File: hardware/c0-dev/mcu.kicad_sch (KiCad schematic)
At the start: 43 parts, among them J15 TAG_CONNECT, J17 PinHeader_2.54mm, U7 TCA9555PWR, U8 W25Q128JVP, U9 RP2350A, Y1 ABM8-272-T3 (12Mhz)

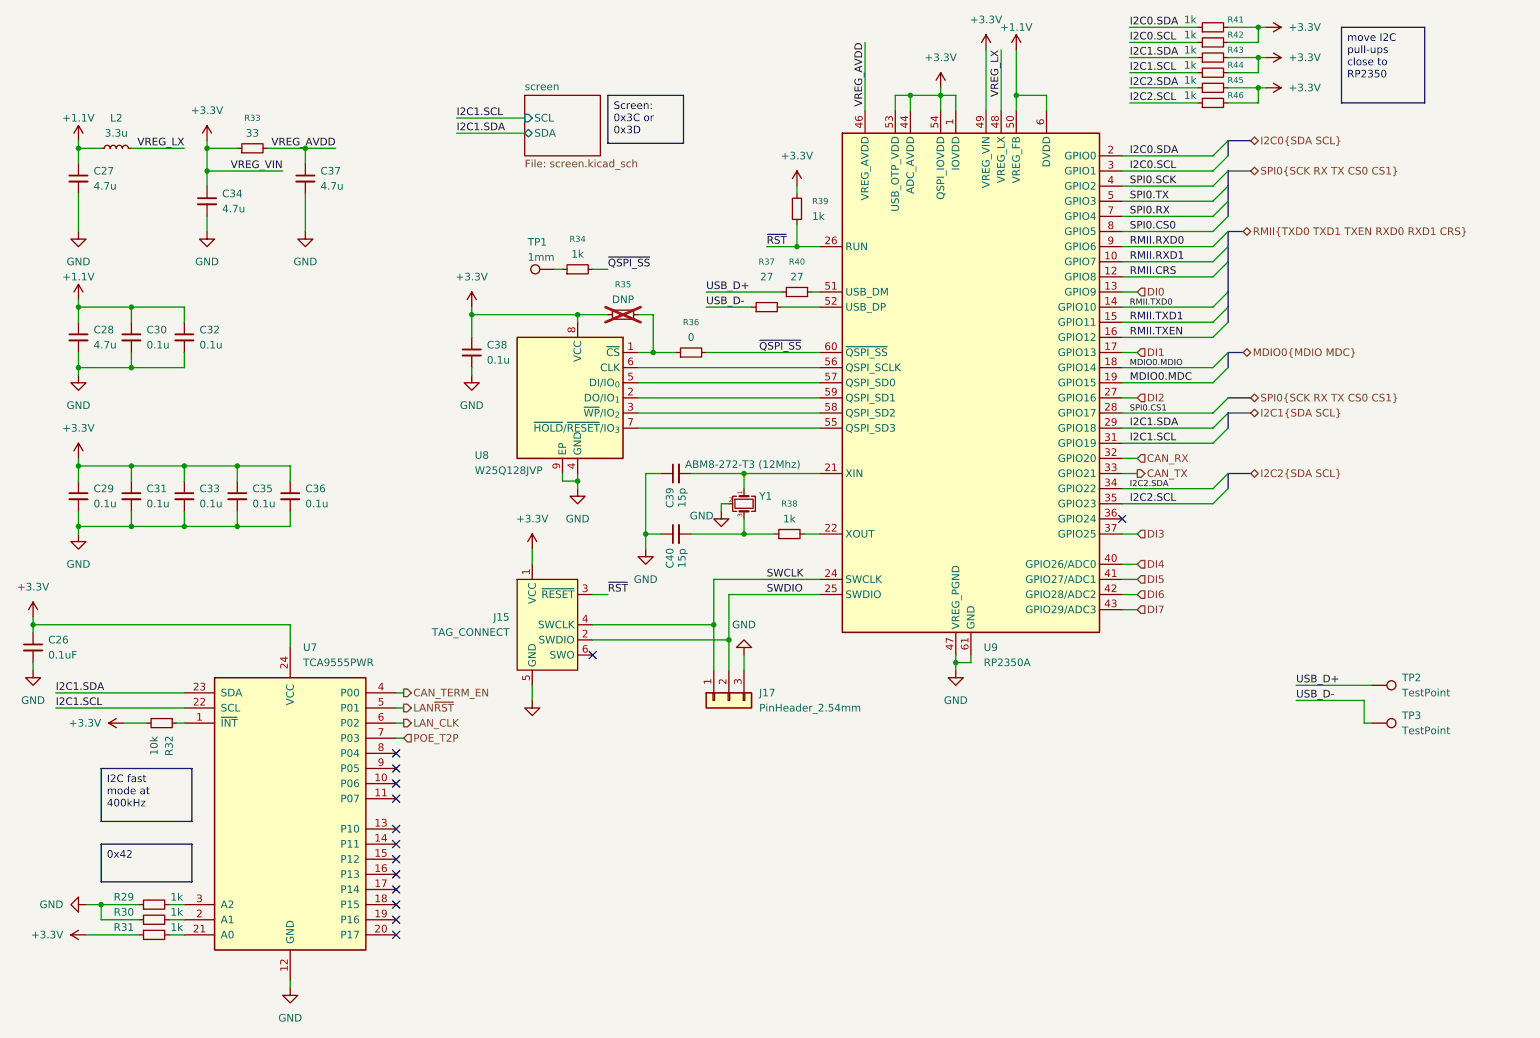
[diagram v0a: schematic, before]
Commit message: added watchdog
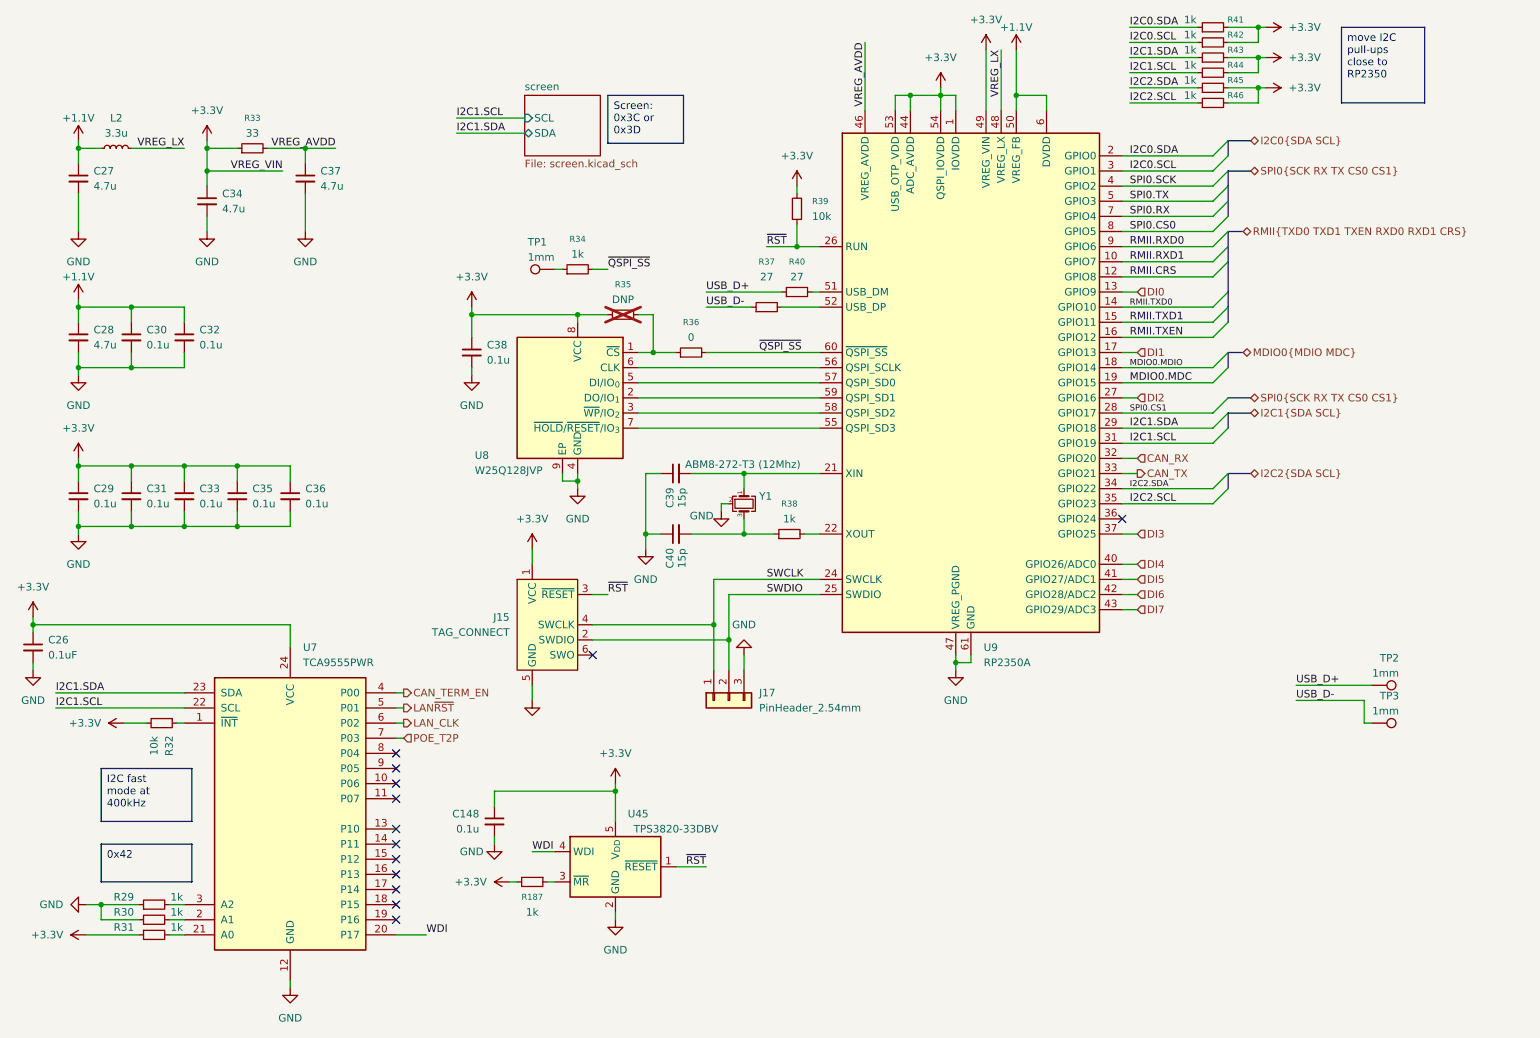
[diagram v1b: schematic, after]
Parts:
- added C148: 0.1u, Capacitor_SMD:C_0402_1005Metric, symbol Device:C_Small
- added R187: 1k, Resistor_SMD:R_0402_1005Metric, symbol Device:R_Small
- added U45: TPS3820-33DBV, Package_TO_SOT_SMD:SOT-23-5, symbol Power_Supervisor:TPS3823-xxDBV
- R39: value 1k -> 10k
- TP2, TP3: value TestPoint -> 1mm; footprint TestPoint:TestPoint_Pad_D2.0mm -> TestPoint:TestPoint_Pad_D1.0mm
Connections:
- net +3.3V: now also C148.1, R187.2, U45.5 (V_{DD})
- net GND: now also C148.2, U45.2 (GND)
- net ~{RST}: now also U45.1 (~{RESET})
- net WDI: now reaches U7.20 (P17)
- net WDI: now also U45.4 (WDI)
- new net: R187.1, U45.3 (~{MR})
- no-connect marks 14 -> 13

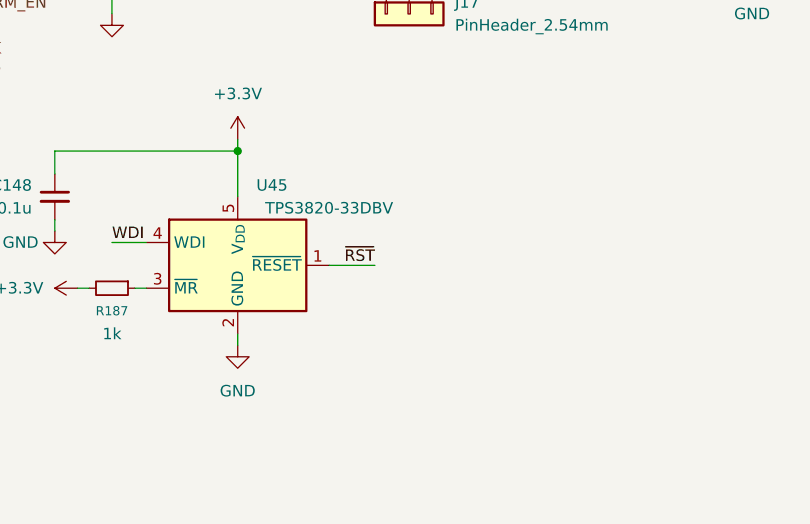
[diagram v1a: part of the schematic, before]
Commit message: added watchdog output disable
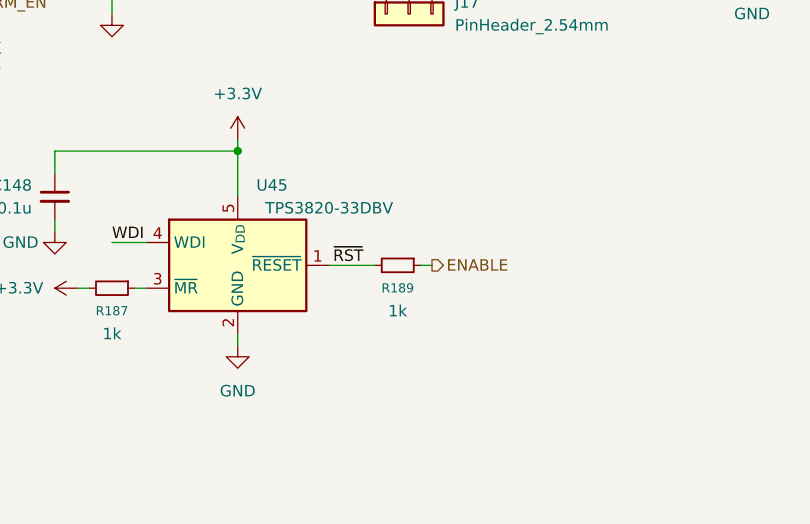
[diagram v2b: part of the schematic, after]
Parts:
- added R189: 1k, Resistor_SMD:R_0402_1005Metric, symbol Device:R_Small
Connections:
- net ~{RST}: now also R189.2
- new net ENABLE: R189.1
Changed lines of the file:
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@@
 	(wire
 		(pts
+			(xy 153.67 163.83) (xy 154.94 163.83)
+		)
+		(stroke
+			(width 0)
+			(type default)
+		)
+	)
+	(wire
+		(pts
 			(xy 219.71 22.86) (xy 231.14 22.86)
 		)
@@
 		)
 	)
+	(label "~{RST}"
+		(at 147.32 163.83 180)
+		(effects
+			(font
+				(size 1.27 1.27)
+			)
+			(justify right bottom)
+		)
+	)
 	(label "I2C1.SCL"
 		(at 219.71 30.48 0)
@@
 		)
 	)
-	(label "~{RST}"
-		(at 148.59 163.83 180)
-		(effects
-			(font
-				(size 1.27 1.27)
-			)
-			(justify right bottom)
-		)
-	)
 	(hierarchical_label "MDIO0{MDIO MDC}"
 		(shape bidirectional)
@@
 		)
 	)
+	(hierarchical_label "ENABLE"
+		(shape output)
+		(at 154.94 163.83 0)
+		(effects
+			(font
+				(size 1.27 1.27)
+			)
+			(justify left)
+		)
+	)
 	(hierarchical_label "CAN_TERM_EN"
 		(shape output)
@@
 					(unit 1)
 				)
+			)
+		)
+	)
+	(symbol
+		(lib_id "Device:R_Small")
+		(at 151.13 163.83 270)
+		(unit 1)
+		(body_style 1)
+		(exclude_from_sim no)
+		(in_bom yes)
+		(on_board yes)
+		(in_pos_files yes)
+		(dnp no)
+		(property "Reference" "R189"
+			(at 151.13 166.37 90)
+			(show_name no)
+			(do_not_autoplace no)
+			(effects
+				(font
+					(size 1.016 1.016)
+				)
+			)
+		)
+		(property "Value" "1k"
+			(at 151.13 168.91 90)
+			(show_name no)
+			(do_not_autoplace no)
+			(effects
+				(font
+					(size 1.27 1.27)
+				)
+			)
+		)
+		(property "Footprint" "Resistor_SMD:R_0402_1005Metric"
+			(at 151.13 163.83 0)
+			(hide yes)
+			(show_name no)
+			(do_not_autoplace no)
+			(effects
+				(font
+					(size 1.27 1.27)
+				)
+			)
+		)
+		(property "Datasheet" ""
+			(at 151.13 163.83 0)
+			(hide yes)
+			(show_name no)
+			(do_not_autoplace no)
+			(effects
+				(font
+					(size 1.27 1.27)
+				)
+			)
+		)
+		(property "Description" "Resistor, small symbol"
+			(at 151.13 163.83 0)
+			(hide yes)
+			(show_name no)
+			(do_not_autoplace no)
+			(effects
+				(font
+					(size 1.27 1.27)
+				)
+			)
+		)
+		(pin "2"
+		)
+		(pin "1"
+		)
+		(instances
+			(project "c0-dev"
+				(path "/b8347a0e-ad04-4414-969d-3c64a611d74e/b3a362d3-bb15-48bf-a1e5-1773c27a02b7"
+					(reference "R189")
+					(unit 1)
+				)

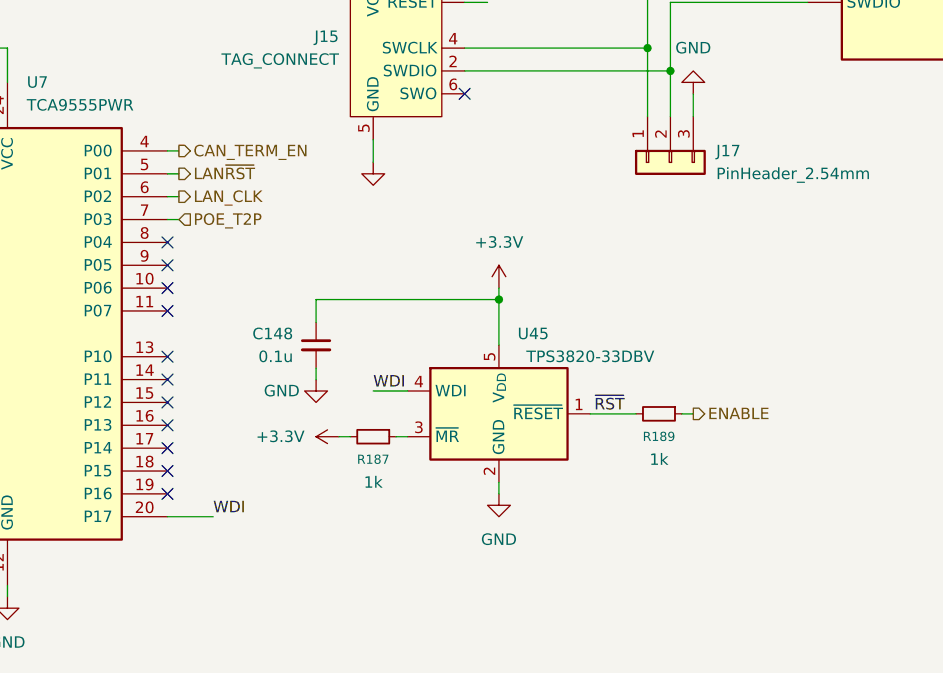
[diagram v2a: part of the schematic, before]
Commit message: added status leds
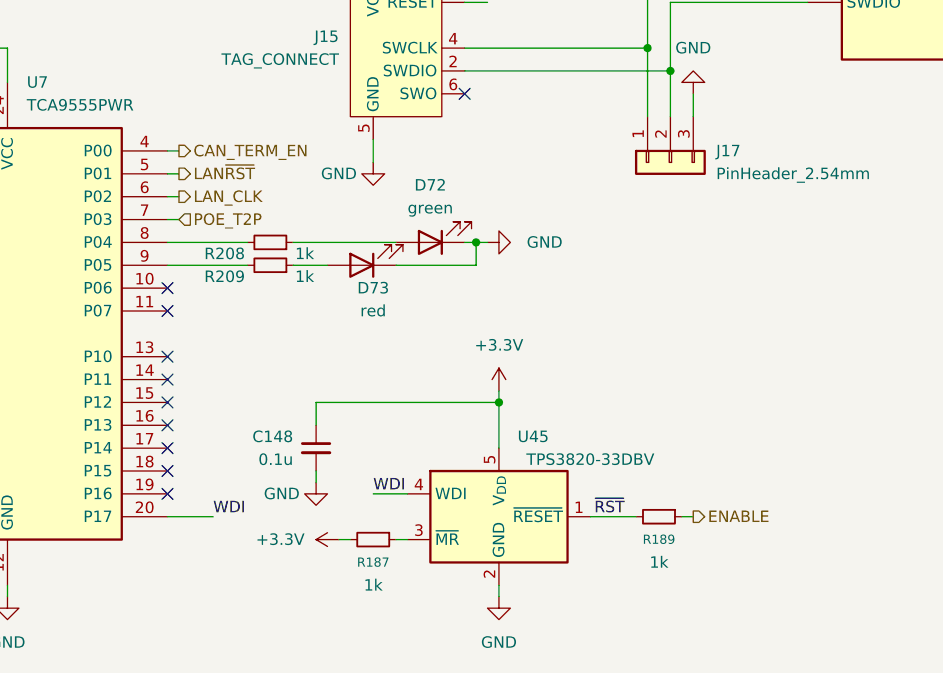
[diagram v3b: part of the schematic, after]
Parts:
- added D72: green, LED_SMD:LED_0402_1005Metric, symbol Device:LED
- added D73: red, LED_SMD:LED_0402_1005Metric, symbol Device:LED
- added R208, R209: 1k, Resistor_SMD:R_0402_1005Metric, symbol Device:R_Small
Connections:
- net GND: now also D72.1 (K), D73.1 (K)
- net at U7.8 (P04): now also R208.2
- net at U7.9 (P05): now also R209.2
- new net: D73.2 (A), R209.1
- new net: D72.2 (A), R208.1
- no-connect marks 13 -> 11
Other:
- moved on the sheet: C148, R187, R189, U45

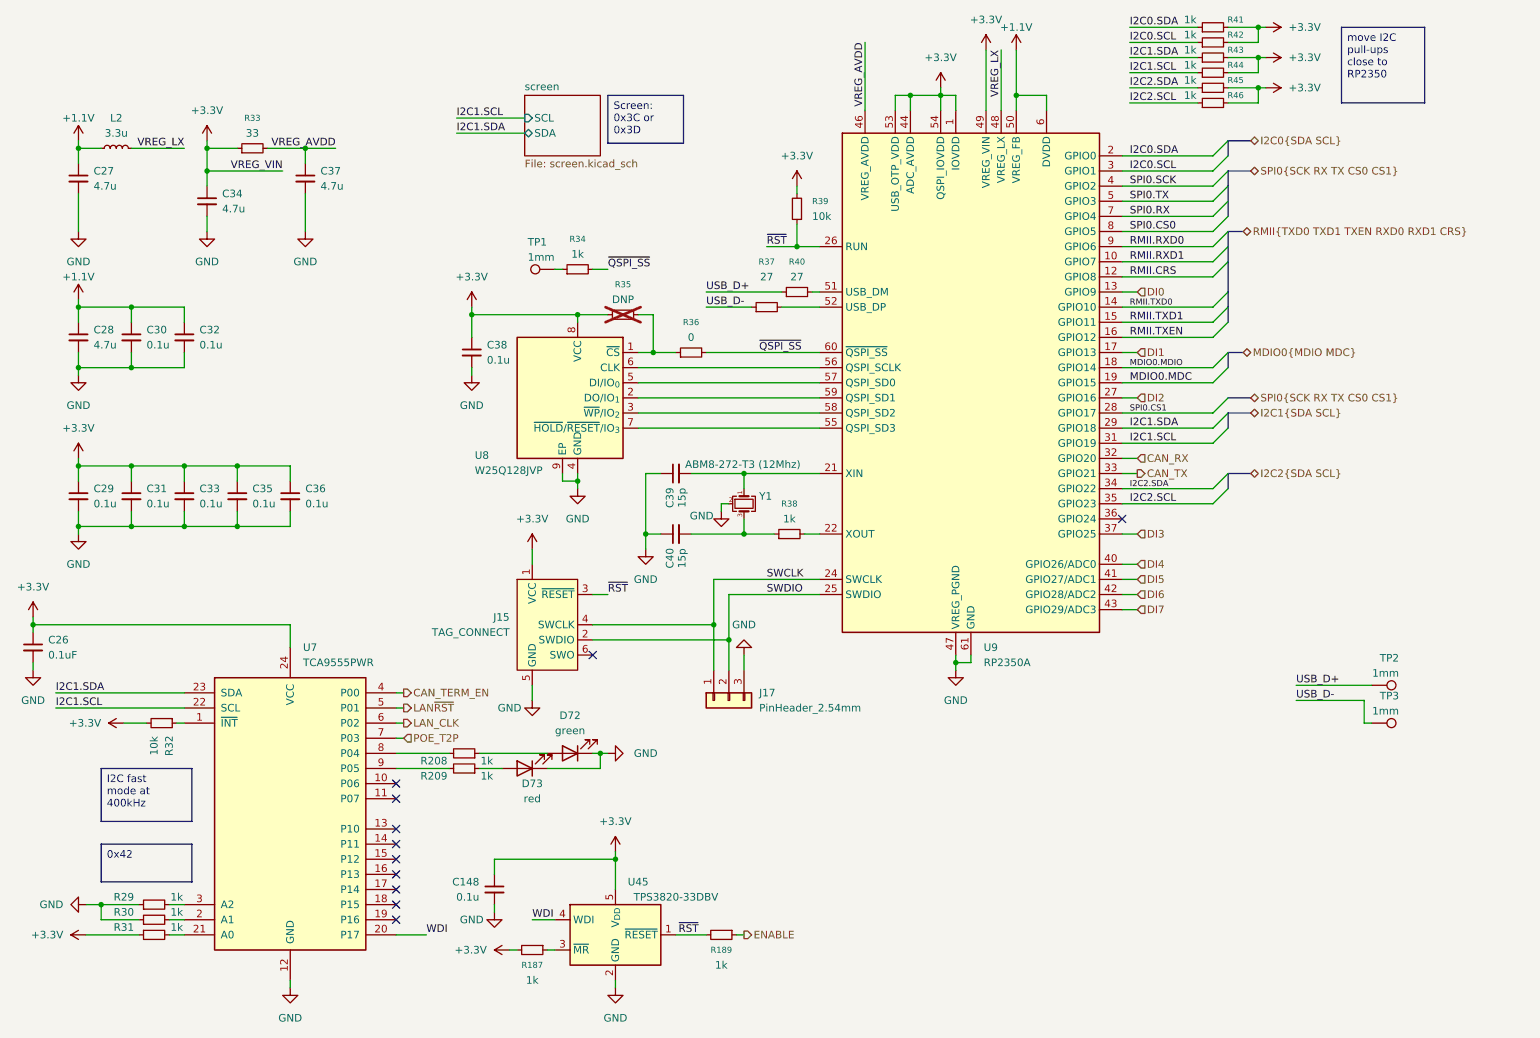
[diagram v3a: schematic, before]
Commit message: added 4-pin connector
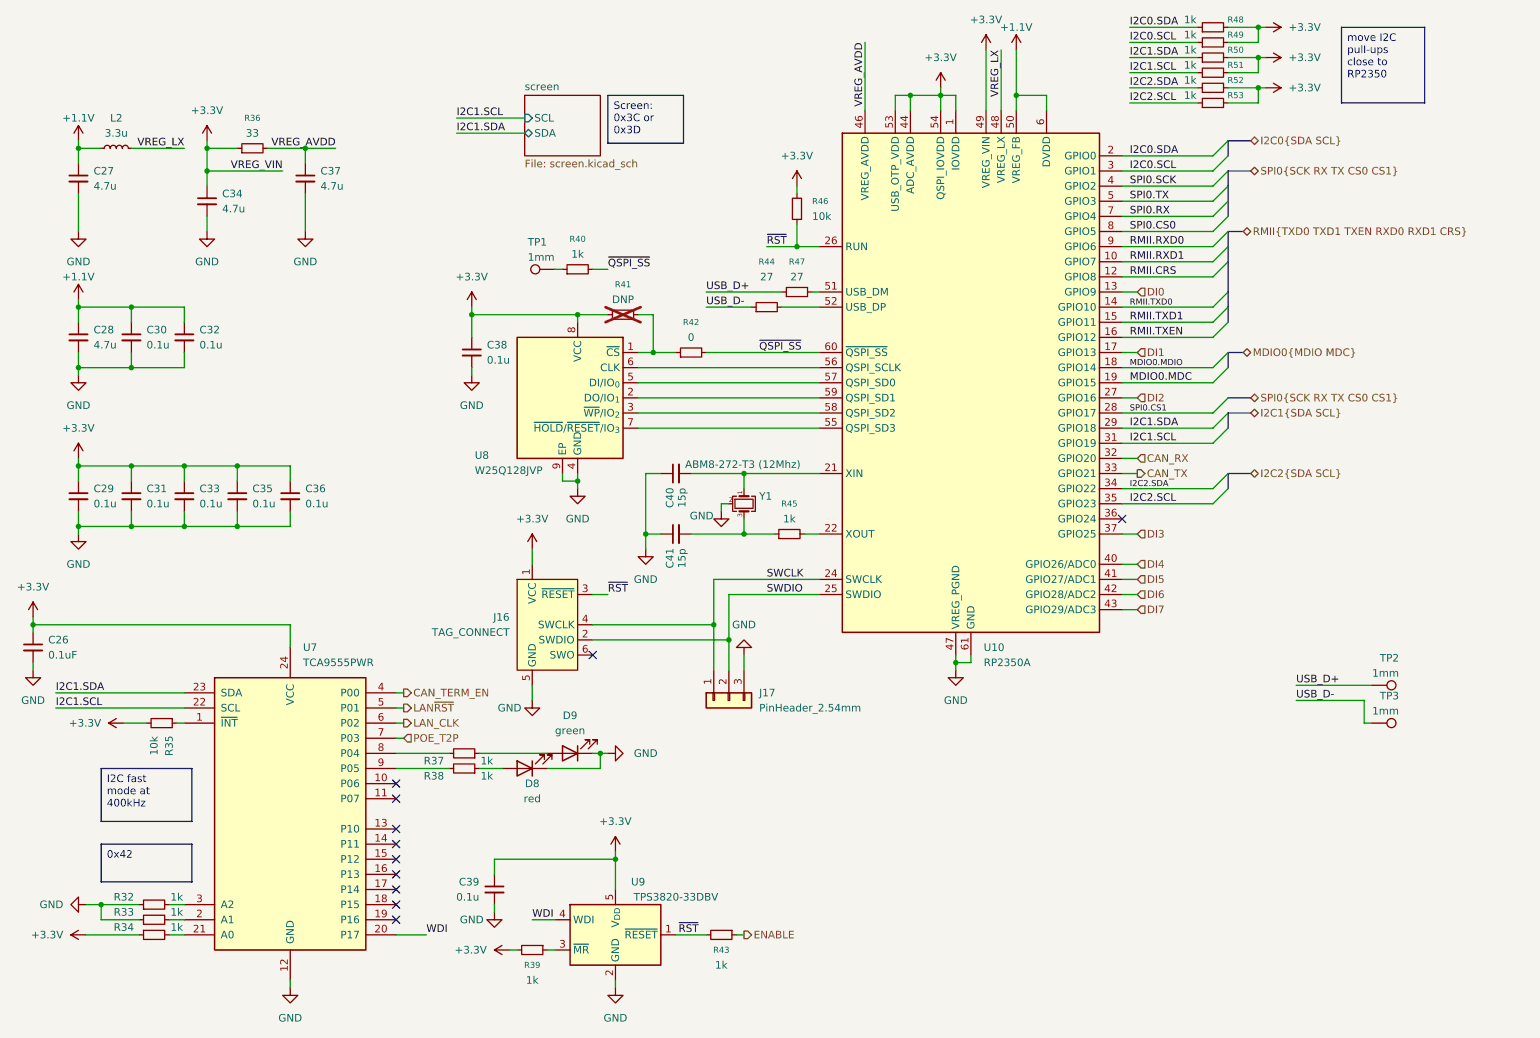
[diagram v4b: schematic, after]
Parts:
- renumbered C148 to C39, C39 to C40, C40 to C41, D73 to D8, D72 to D9, J15 to J16, R29 to R32, R30 to R33, R31 to R34, R32 to R35, R33 to R36, R208 to R37, R209 to R38, R187 to R39, R34 to R40, R35 to R41, R36 to R42, R189 to R43, R37 to R44, R38 to R45, R39 to R46, R40 to R47, R41 to R48, R42 to R49, R43 to R50, R44 to R51, R45 to R52, R46 to R53, U9 to U10, U45 to U9
